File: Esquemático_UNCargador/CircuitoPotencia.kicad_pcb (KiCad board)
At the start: 2 copper layers, 28.4 x 71.9 mm, 56 parts, among them IC1 LF353, J1 Conn_01x08_Pin, J2 Relay1, J3 Conn_02x03_Counter_Clockwise, J4 GFCI, J5 PZEM 004T 100A, J6 NTC 3950, J8 Conn_01x02_Pin, J9 Relay2, Q1 PN2222A, Q2 PN2222A, SW1 SW_Push, SW2 SW_Push, SW3 SW_Push, SW4 SW_Push, SW5 SW_Push, U3 LM7912(Inversor)

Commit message: version inicial layout PCB
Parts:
- removed PS1: BAC05S05DC, Convertidor_AC-DC:AC-DC_Converter
- added D8: SMAZ5V1, Esquemático_UNCargador:DO-214AC, F.Cu at (146.9, 94.8)
- added D9: SMAZ5V1, Esquemático_UNCargador:DO-214AC, F.Cu at (146.9, 99.1)
- added PT1: BAC05S05DC, Convertidor_AC-DC:AC-DC_Converter, F.Cu at (60.2, 77.0)
- added U1: LM324N, LM324:DIP794W45P254L1969H508Q14, F.Cu at (140.6, 125.7)
- added U_3.3V1: LM2596_3.3V, LM2596ADJ:LM2596ADJ, F.Cu at (97.8, 69.4)
- added U_5V1: LM2596_5V, LM2596ADJ:LM2596ADJ, F.Cu at (72.1, 45.7)
- J1: value Conn_01x08_Pin -> Conn_01x04_Pin; footprint Connector_PinHeader_2.54mm:PinHeader_1x08_P2.54mm_Vertical -> Connector_PinHeader_2.54mm:PinHeader_1x04_P2.54mm_Vertical
- moved J1 133.0 mm to (55.4, 134.9)
- moved SW1 123.8 mm to (89.9, 142.9)
- moved SW2 123.8 mm to (94.6, 142.9)
- moved SW3 123.8 mm to (99.2, 142.9)
- moved SW4 123.8 mm to (103.9, 142.9)
- moved SW5 123.8 mm to (108.5, 142.9)
- moved C6 122.0 mm to (55.4, 113.1)
- moved C7 122.0 mm to (55.4, 122.7)
- moved A1 118.5 mm to (83.9, 146.7), turned to 180 degrees
- moved CIn3 115.8 mm to (103.5, 23.9)
- moved J5 105.7 mm to (160.8, 92.9)
- moved CIn4 104.0 mm to (104.5, 39.1)
- moved Input110 100.2 mm to (75.4, 20.1), turned to 180 degrees
- moved JP1 99.7 mm to (125.5, 18.5), turned to -90 degrees
- moved U3 99.0 mm to (104.4, 48.8)
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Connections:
- net CLK renamed DIsplaySCL
- J1 pad 3: SDA -> DisplaySDA
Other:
- board size 28.4 x 71.9 mm -> 135.4 x 138.9 mm

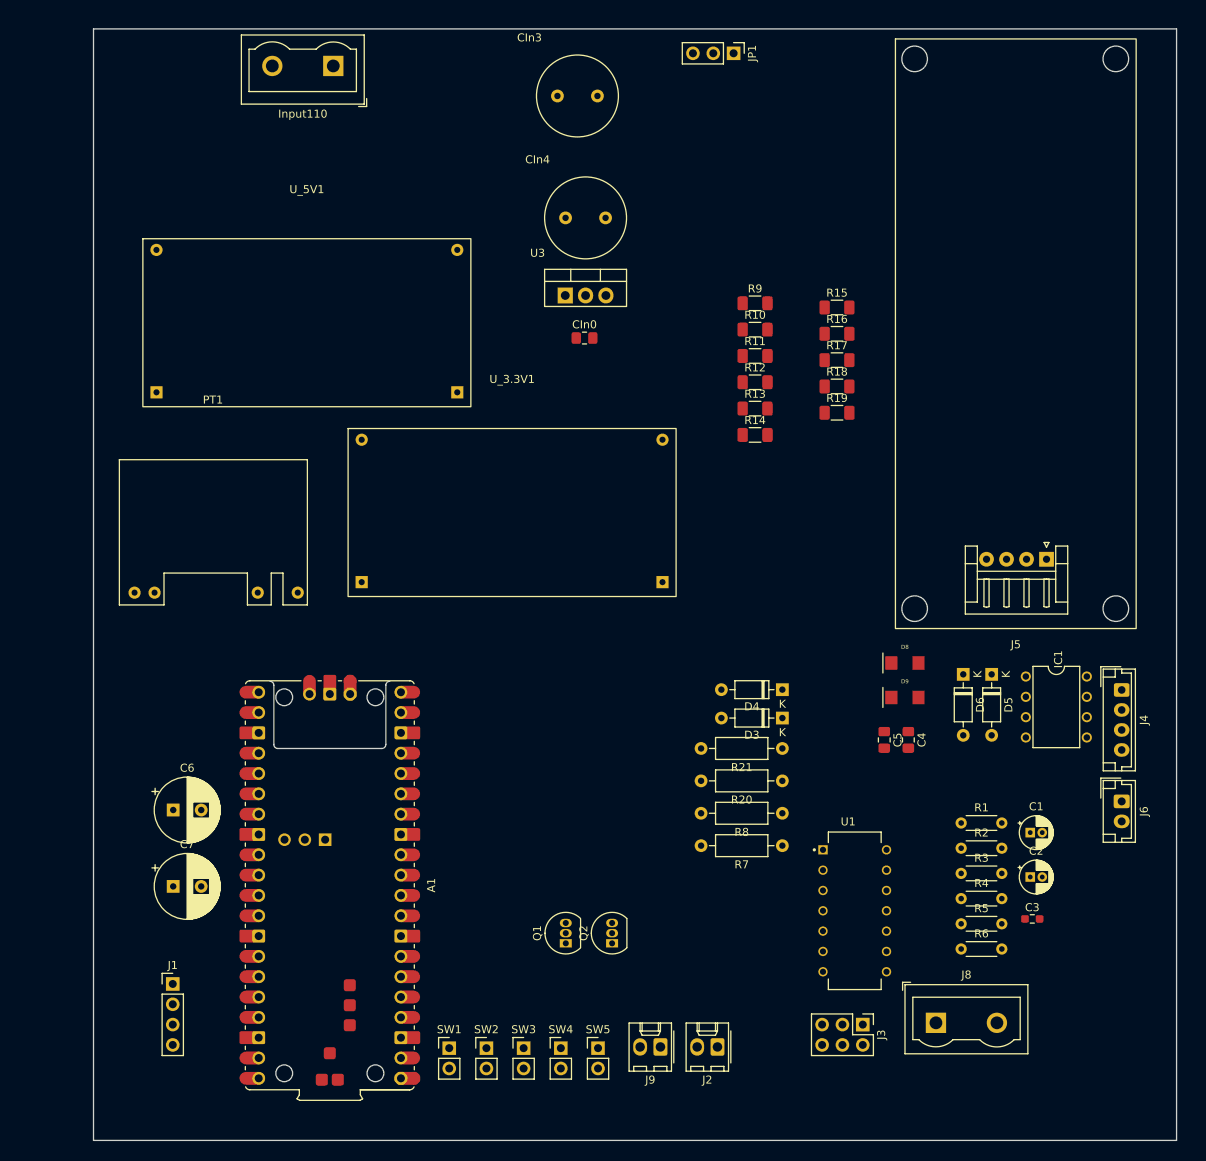
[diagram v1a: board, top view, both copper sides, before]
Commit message: PCB con ruteo realizado. Errores en los anchos de vias -0.2mm. Huella LF356n actualizada
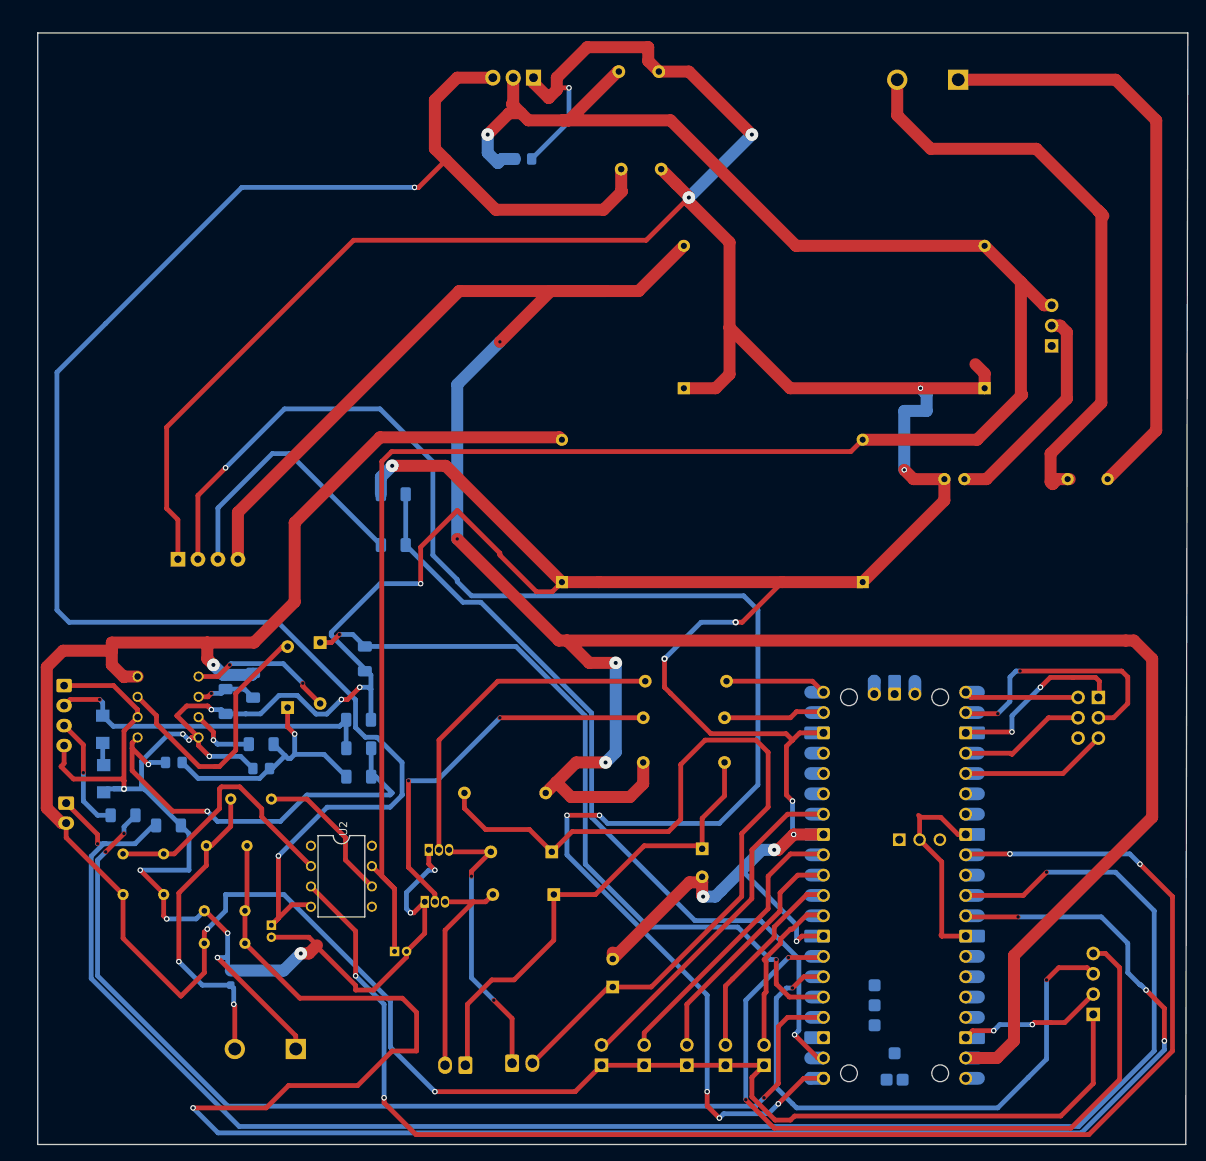
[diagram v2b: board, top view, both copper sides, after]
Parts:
- removed U1: LM324N, LM324:DIP794W45P254L1969H508Q14
- added U2: LF356, LF353:DIL08, F.Cu at (76.5, 121.4)
- A1, C1, C2, C3, C4, C5, C6, C7, CIn0, CIn3, CIn4, D3, D4, D5, D6, D8, D9, IC1, Input110, J1, J2, J3, J4, J5, J6, J8, J9, JP1, PT1, Q1, Q2, R1, R10, R11, R12, R13, R14, R15, R16, R17, R18, R19, R2, R20, R21, R3, R4, R5, R6, R7, R8, R9, SW1, SW2, SW3, SW4, SW5, U3, U_3.3V1, U_5V1: moved to B.Cu
- moved J4 132.2 mm to (41.8, 97.6)
- moved J6 131.9 mm to (42.0, 112.3)
- moved J1 115.1 mm to (170.4, 138.7)
- moved IC1 111.0 mm to (54.8, 100.3)
- moved R1 105.1 mm to (49.2, 123.7), turned to 90 degrees
- moved R17 101.8 mm to (54.8, 115.1), turned to 180 degrees
- moved PT1 101.3 mm to (161.4, 80.8)
- moved D8 101.2 mm to (46.7, 109.2), turned to 90 degrees
- moved J5 100.9 mm to (59.9, 92.9), turned to 180 degrees
- moved C3 100.5 mm to (62.6, 134.1), turned to -90 degrees
- moved D9 100.4 mm to (46.6, 103.0), turned to -90 degrees
- moved R2 99.7 mm to (54.2, 118.6), turned to -90 degrees
- moved R10 99.6 mm to (49.2, 113.8)
- moved C2 95.1 mm to (67.7, 127.5), turned to -90 degrees
- moved R6 94.6 mm to (59.3, 129.8)
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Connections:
- A1 pad 29: Pilot_PWM -> /Microcontrolador/Pilot_PWM
- J1 pad 4: DIsplaySCL -> DisplaySCL
- J5 pad 2: /Sensores1/RX_Pzem -> /Microcontrolador/TX_Pzem
- R12 pad 1: /Sensores1/TX_Pzem -> /Microcontrolador/RX_Pzem
- R13 pad 2: /Sensores1/TX_Pzem -> /Microcontrolador/RX_Pzem
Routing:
- net GND: track 0.00 -> 772.5 mm, vias 0 -> 32
- net +5V: track 0.00 -> 317.3 mm, vias 0 -> 4
- net +3.3V: track 0.00 -> 301.8 mm, vias 0 -> 3
- net +12V: track 0.00 -> 266.0 mm, vias 0 -> 1
- net Pilot_ADC: track 0.00 -> 237.0 mm, vias 0 -> 4
- net -12V: track 0.00 -> 225.1 mm, vias 0 -> 2
- net /Microcontrolador/NTC_Analog: track 0.00 -> 221.8 mm, vias 0 -> 2
- net /Microcontrolador/TX_Pzem: track 0.00 -> 208.8 mm, vias 0 -> 6
- net /Microcontrolador/Pilot_PWM: track 0.00 -> 182.8 mm, vias 0 -> 4
- net /Microcontrolador/GFCI_TEST: track 0.00 -> 128.3 mm, vias 0 -> 3
- net Net-(D3-K): track 0.00 -> 106.8 mm
- net /Microcontrolador/RX_Pzem: track 0.00 -> 99.1 mm, vias 0 -> 1
- net /Microcontrolador/FALLA: track 0.00 -> 95.4 mm, vias 0 -> 2
- net DisplaySCL: track 0.00 -> 93.2 mm, vias 0 -> 2
- net /Potencia2.0/N: track 0.00 -> 74.9 mm
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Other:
- board size 135.4 x 138.9 mm -> 143.8 x 138.9 mm

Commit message: PCB con Modificaciones de PLanos de Tierra y Huecos de soporte
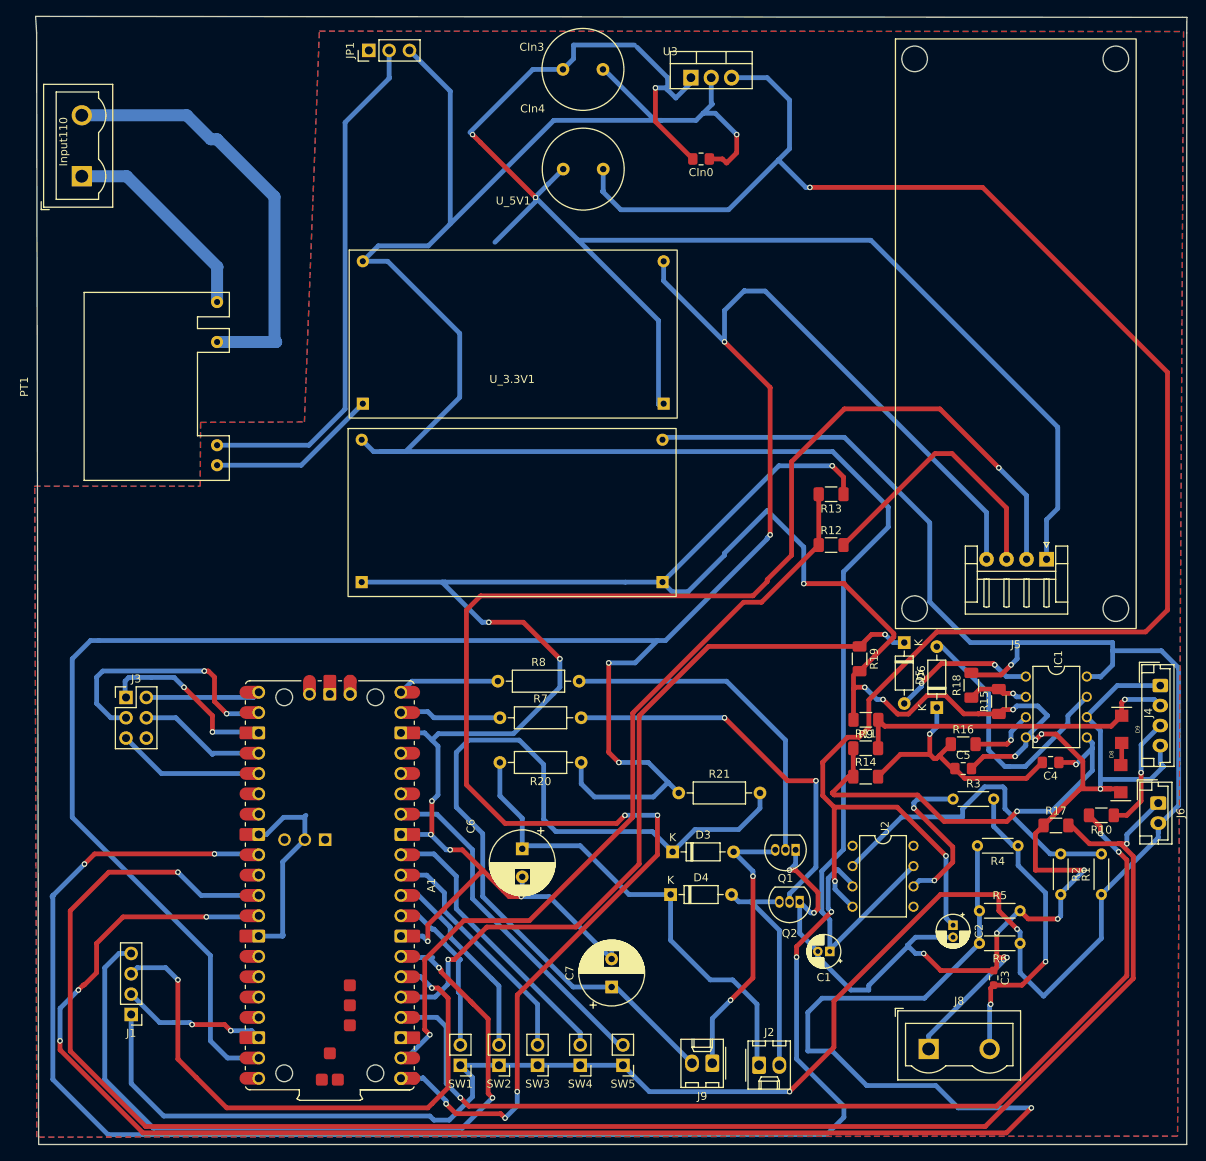
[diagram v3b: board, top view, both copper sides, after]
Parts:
- A1, C1, C2, C3, C4, C5, C6, C7, CIn0, CIn3, CIn4, D3, D4, D5, D6, D8, D9, IC1, Input110, J1, J2, J3, J4, J5, J6, J8, J9, JP1, PT1, Q1, Q2, R1, R10, R11, R12, R13, R14, R15, R16, R17, R18, R19, R2, R20, R21, R3, R4, R5, R6, R7, R8, R9, SW1, SW2, SW3, SW4, SW5, U3, U_3.3V1, U_5V1: moved to F.Cu
- moved J4 137.0 mm to (178.8, 97.6)
- moved J6 136.5 mm to (178.6, 112.3)
- moved D9 127.4 mm to (174.0, 103.0)
- moved D8 127.1 mm to (173.9, 109.2)
- moved R1 122.3 mm to (171.4, 123.7)
- moved R10 122.3 mm to (171.4, 113.8), turned to 180 degrees
- moved J3 121.5 mm to (49.5, 99.1), turned to 0 degrees
- moved J1 120.3 mm to (50.2, 138.7), turned to 180 degrees
- moved R2 112.1 mm to (166.4, 118.6)
- moved PT1 111.4 mm to (51.9, 60.4), turned to 90 degrees
- moved IC1 111.0 mm to (165.8, 100.3)
- moved R17 110.9 mm to (165.8, 115.1), turned to 0 degrees
- moved Input110 110.2 mm to (44.0, 33.9), turned to 90 degrees
- moved C4 109.6 mm to (165.1, 107.2), turned to 180 degrees
- moved R6 102.0 mm to (161.3, 129.8), turned to 180 degrees
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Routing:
- net GND: track 772.5 -> 720.7 mm, vias 32 -> 30
- net /Potencia2.0/In110v: track 74.2 -> 26.1 mm
- net Net-(JP1-C): track 27.5 -> 65.0 mm
- net +5V: track 317.3 -> 294.6 mm
- net /Potencia2.0/N: track 74.9 -> 53.9 mm
- net +12V: track 266.0 -> 280.4 mm
- net /Microcontrolador/Pilot_PWM: track 182.8 -> 192.6 mm
- net Net-(U2--): track 33.1 -> 40.7 mm
- net -12V: track 225.1 -> 232.3 mm, vias 2 -> 3
- net DisplaySCL: track 93.2 -> 96.8 mm
- net Net-(R3-Pad1): track 18.7 -> 20.7 mm, vias 0 -> 2
- net +3.3V: track 301.8 -> 303.3 mm
- added copper zone on B.Cu, net GND
- added copper zone on F.Cu, net GND
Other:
- board size 143.8 x 138.9 mm -> 143.9 x 141 mm
